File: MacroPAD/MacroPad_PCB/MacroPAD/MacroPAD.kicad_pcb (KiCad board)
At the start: 4 copper layers, 81.9 x 106.5 mm, 54 parts, among them J1 USB_C_Receptacle_USB2.0_16P, SW1 SW_Push, SW2 RotaryEncoder, U1 ATmega32U4-A, U2 USB6B1, Y1 Crystal

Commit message: Changing c-type input with differential pairs
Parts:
- added U3: RS3E075ATTB, RS3E075ATTB:TRANS_RRH040P_ROM, F.Cu at (160.4, 60.7)
- R2, R3: footprint Resistor_SMD:R_1206_3216Metric -> Resistor_SMD:R_0603_1608Metric
- moved R7 19.3 mm to (156.0, 54.1)
- moved D14 19.3 mm to (158.6, 54.1)
- moved J1 4.64 mm to (167.0, 69.8)
- moved R2 4.31 mm to (147.8, 70.7)
- moved R4 2.71 mm to (155.9, 74.3)
- moved U2 2.52 mm to (155.0, 69.9)
- moved R5 2.24 mm to (157.3, 65.3)
- moved R3 1.67 mm to (147.8, 69.1)
- moved D10 0.21 mm to (97.9, 78.0)
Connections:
- net Net-(J1-D+-PadA6) renamed /D+
- net Net-(J1-D--PadA7) renamed /D-
- J1 pad A4: AVCC -> Net-(J1-VBUS-PadA4)
- J1 pad A9: AVCC -> Net-(J1-VBUS-PadA4)
- J1 pad B4: AVCC -> Net-(J1-VBUS-PadA4)
- J1 pad B9: AVCC -> Net-(J1-VBUS-PadA4)
- R2 pad 1: D+ -> /D_OUT-
- R2 pad 2: Net-(U1-D+) -> /D_N
- R3 pad 1: D- -> /D_OUT+
- R3 pad 2: Net-(U1-D-) -> /D_P
- U1 pad 3: Net-(U1-D-) -> /D_N
- U1 pad 4: Net-(U1-D+) -> /D_P
- U2 pad 6: D+ -> /D_OUT+
- U2 pad 7: D- -> /D_OUT-
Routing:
- net Net-(J1-VBUS-PadA4): track 0.00 -> 19.2 mm
- net AVCC: track 66.9 -> 53.0 mm
- net Net-(U1-D+): track 9.33 -> 0.00 mm
- net /D_P: track 0.00 -> 7.82 mm
- net /D_N: track 0.00 -> 7.78 mm
- net Net-(U1-D-): track 7.28 -> 0.00 mm
- net D-: track 4.41 -> 0.00 mm
- net /D_OUT-: track 0.00 -> 4.25 mm
- net /D_OUT+: track 0.00 -> 4.25 mm
- net D+: track 2.91 -> 0.00 mm
- net GND: track 59.7 -> 61.6 mm, vias 28 -> 29
- net /D+: track 9.25 -> 7.60 mm
- net Net-(J1-CC1): track 8.15 -> 6.88 mm
- net /D-: track 9.68 -> 8.74 mm
- net Net-(J1-CC2): track 4.96 -> 5.77 mm

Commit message: Fixed C-type
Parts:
- removed U3: RS3E075ATTB, RS3E075ATTB:TRANS_RRH040P_ROM
- J1: value USB_C_Receptacle_USB2.0_16P -> 2171790001; footprint Connector_USB:USB_C_Receptacle_HRO_TYPE-C-31-M-12 -> usb-c-2171790001:MOLEX_2171790001
- moved D14 10.1 mm to (165.5, 61.5)
- moved R7 10.1 mm to (162.8, 61.5)
- moved R5 8.59 mm to (156.9, 73.8), turned to 0 degrees
- moved R4 8.46 mm to (156.7, 65.8)
- moved J1 0.65 mm to (167.6, 69.6)
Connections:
- R4 pad 1: Net-(J1-CC1) -> Net-(J1-CC2)
- R5 pad 1: Net-(J1-CC2) -> GND
- R5 pad 2: GND -> Net-(J1-CC1)
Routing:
- net Net-(J1-VBUS-PadA4): track 19.2 -> 0.00 mm
- net AVCC: track 53.0 -> 47.3 mm, vias 17 -> 18
- net GND: track 61.6 -> 59.5 mm, vias 29 -> 28
- net /D+: track 7.60 -> 8.93 mm
- net Net-(J1-CC2): track 5.77 -> 6.81 mm
- net /D-: track 8.74 -> 9.62 mm
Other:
- board text added: "MacroPAD V0.1"
- board text added: "Taewoo Kim"

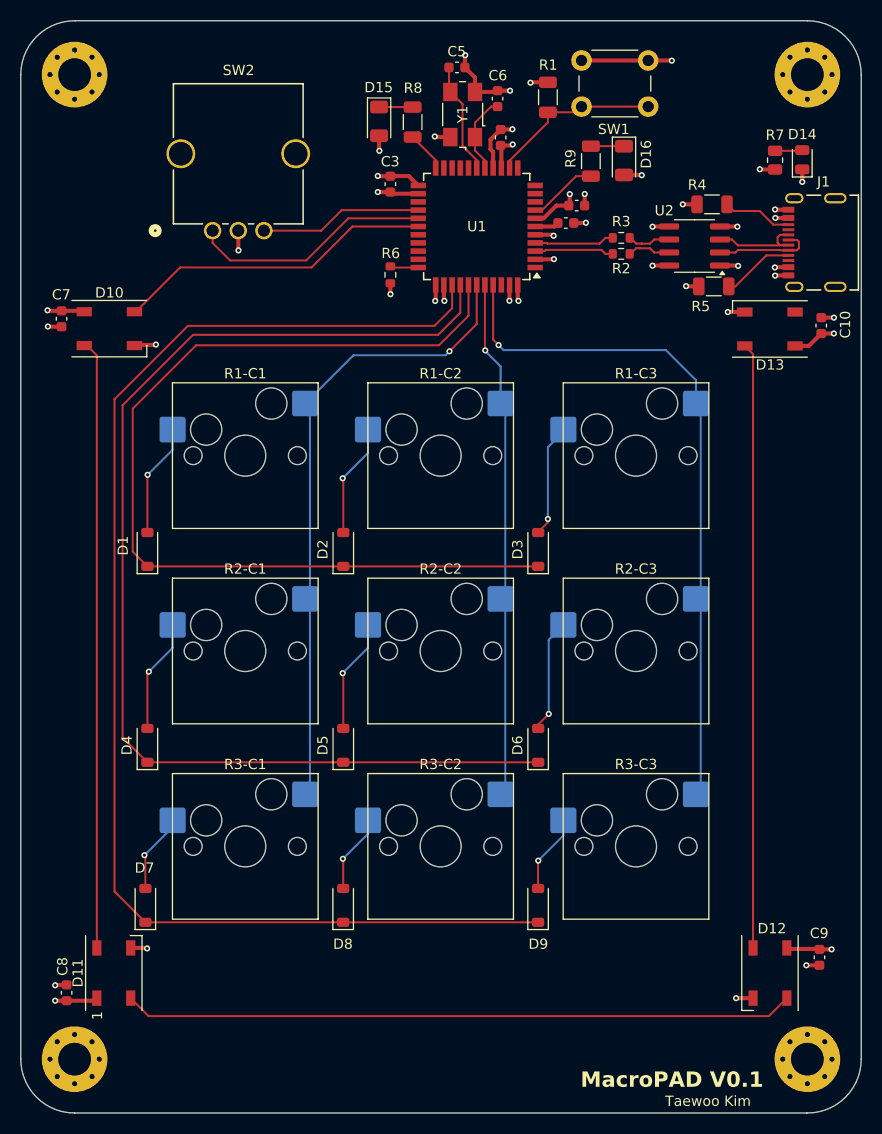
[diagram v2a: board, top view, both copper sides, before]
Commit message: Added ISR Debugg port
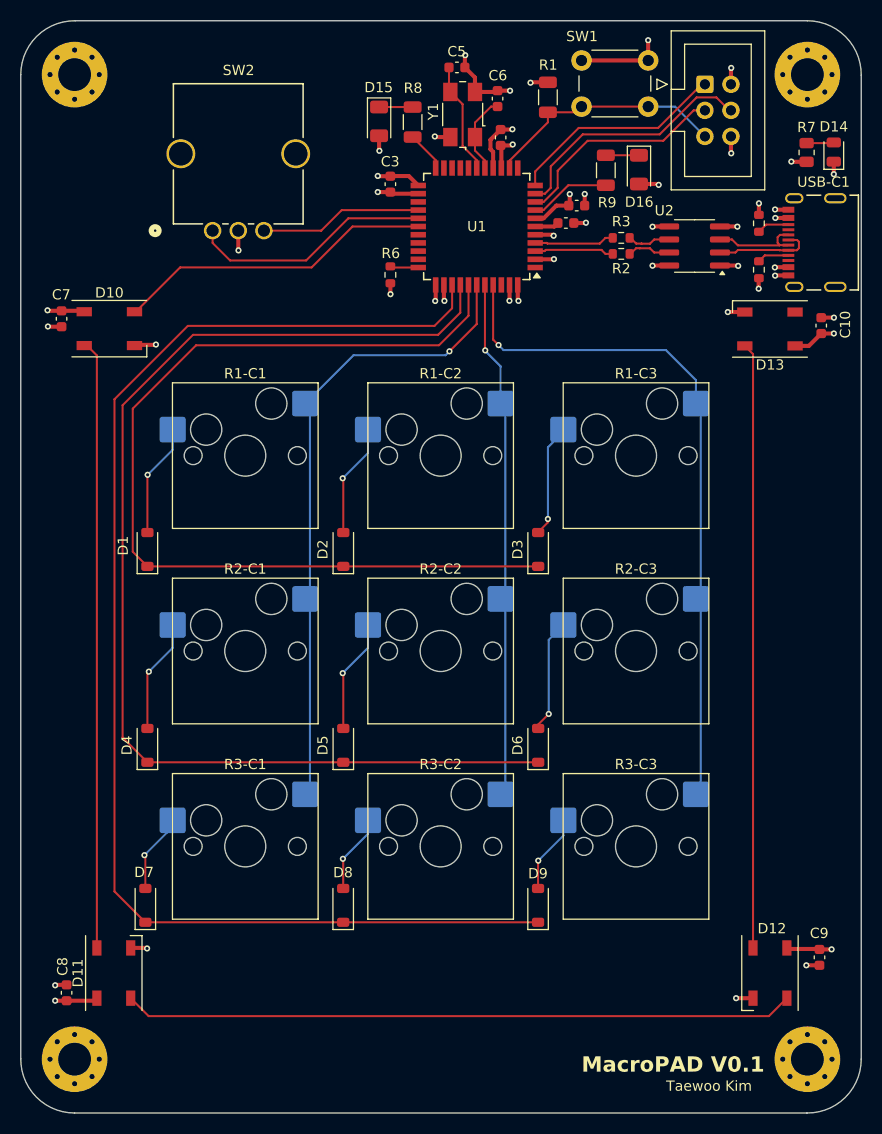
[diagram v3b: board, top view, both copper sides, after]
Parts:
- added J2: AVR-ISP-6, Connector_IDC:IDC-Header_2x03_P2.54mm_Vertical, F.Cu at (156.0, 54.1)
- D1, D2, D3, D4, D5, D6, D7, D8, D9: value D -> 1N4148
- R4, R5: footprint Resistor_SMD:R_1206_3216Metric -> Resistor_SMD:R_0603_1608Metric
- Y1: value Crystal -> 16MHz
- moved R4 4.93 mm to (161.3, 67.7), turned to 90 degrees
- moved R5 4.69 mm to (161.3, 72.2), turned to 90 degrees
- moved R7 3.17 mm to (165.9, 60.8)
- moved D14 3.17 mm to (168.6, 60.8)
- moved D16 1.71 mm to (149.6, 62.5)
- moved R9 1.71 mm to (146.3, 62.5)
- renumbered J1 to USB-C1
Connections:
- net Net-(U1-~{RESET}) renamed ISP_RST
- U1 pad 10: unconnected-(U1-PB2-Pad10) -> MOSI
- U1 pad 11: unconnected-(U1-PB3-Pad11) -> MISO
- U1 pad 9: unconnected-(U1-PB1-Pad9) -> SCK
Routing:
- net MOSI: track 0.00 -> 24.8 mm
- net SCK: track 0.00 -> 21.3 mm
- net MISO: track 0.00 -> 21.3 mm
- net ISP_RST: track 17.0 -> 23.9 mm
- net Net-(USB-C1-CC1): track 7.07 -> 3.11 mm
- net Net-(USB-C1-CC2): track 6.81 -> 3.16 mm
- net AVCC: track 47.3 -> 49.3 mm, vias 18 -> 19
- net Net-(U1-PB0): track 6.80 -> 7.89 mm
- net GND: track 59.5 -> 60.4 mm, vias 28 -> 29

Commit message: Fixed macropad ISR programmer
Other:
- board text added: "ISP-PRG"
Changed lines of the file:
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@@
+		)
+	)
+	(gr_text "ISP-PRG"
+		(at 153.8 66.175 0)
+		(layer "F.SilkS")
+		(effects
+			(font
+				(size 1 1)
+				(thickness 0.1)
+			)
+			(justify left bottom)
 		)
 	)

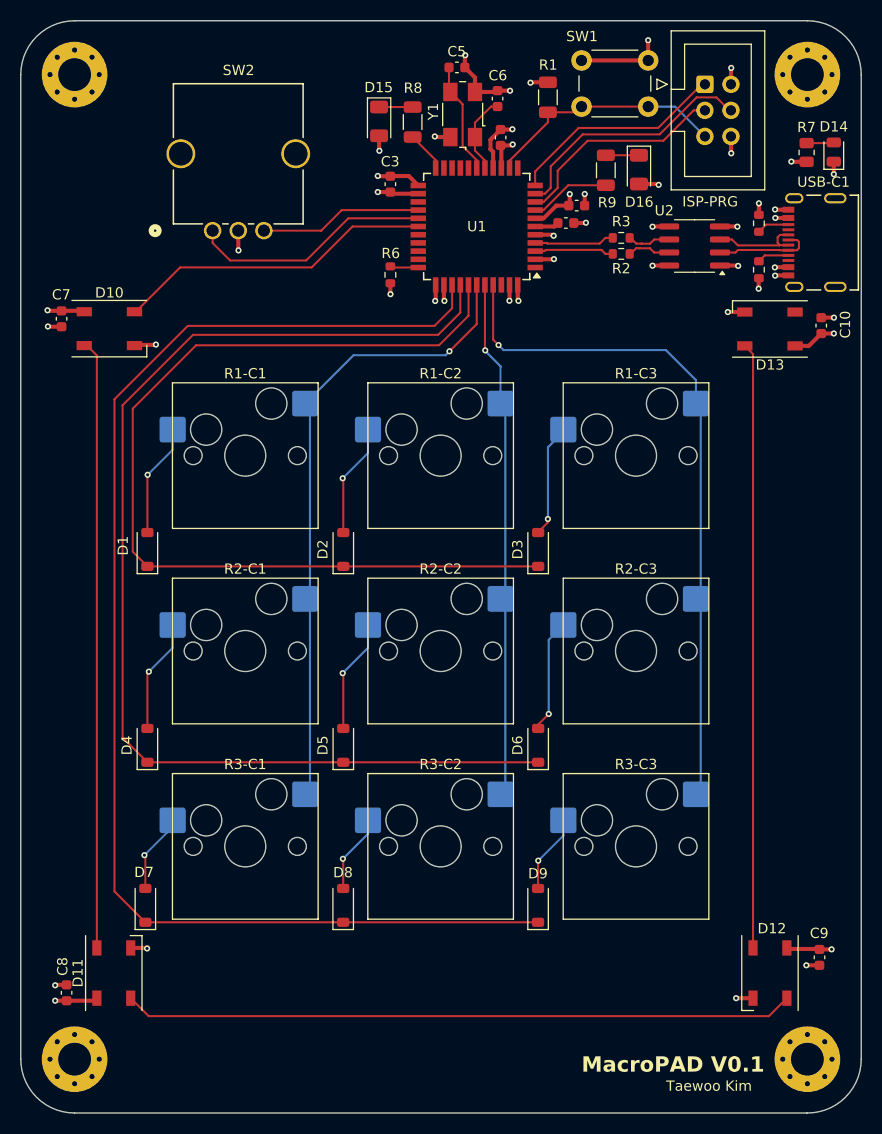
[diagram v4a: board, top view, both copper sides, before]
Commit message: MacroPAD V0.3: Added additional filter for rotary encoder for debounce purpose
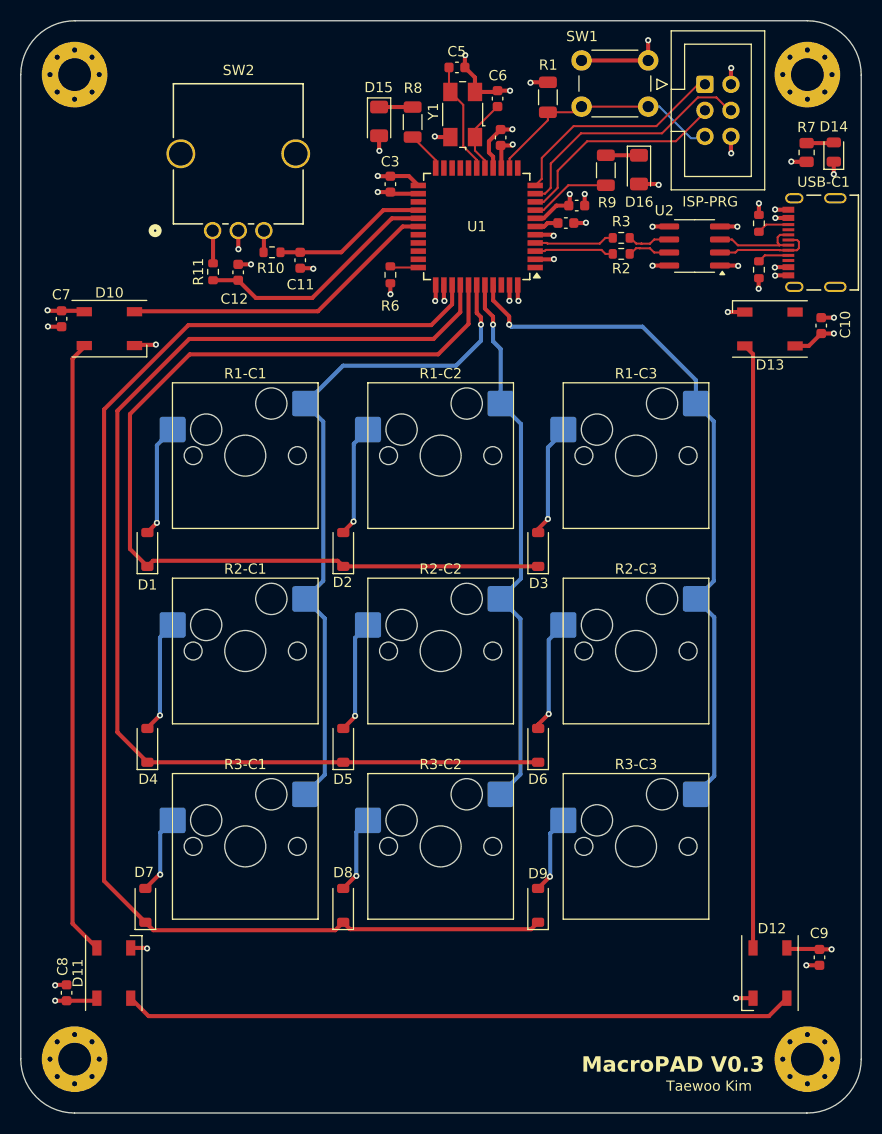
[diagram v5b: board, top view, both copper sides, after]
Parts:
- added C11: 0.01u, Capacitor_SMD:C_0603_1608Metric, F.Cu at (116.5, 71.3)
- added C12: 0.01u, Capacitor_SMD:C_0603_1608Metric, F.Cu at (110.5, 72.5)
- added R10: 10k, Resistor_SMD:R_0603_1608Metric, F.Cu at (113.8, 70.5)
- added R11: 10k, Resistor_SMD:R_0603_1608Metric, F.Cu at (108.0, 72.4)
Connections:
- net AVCC renamed VBUS
- SW2 pad A: ChA -> Net-(R11-Pad2)
- SW2 pad B: ChB -> Net-(R10-Pad1)
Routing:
- net C1: track 62.6 -> 66.4 mm
- net Net-(R11-Pad2): track 0.00 -> 3.20 mm
- net GND: track 60.4 -> 62.9 mm, vias 29 -> 31
- net C2: track 51.1 -> 53.5 mm
- net Net-(R10-Pad1): track 0.00 -> 2.13 mm
- net R3: track 129.4 -> 131.2 mm
- net Net-(D10-DOUT): track 59.2 -> 60.3 mm
- net R1: track 93.6 -> 94.6 mm
- net ChB: track 15.9 -> 15.1 mm
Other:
- board text added: "MacroPAD V0.3"
- board text removed: "MacroPAD V0.1"

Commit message: Added MPN for the BOM
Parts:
- R7, R8, R9: value 1k -> 220
